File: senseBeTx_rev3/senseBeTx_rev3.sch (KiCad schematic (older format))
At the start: 44 parts, among them P1 CONN_02X05, Q1 SI2301, Q2 BC847, Q3 SI2302, Q4 SI2302, Q5 SI2302, Q6 SI2302, Q7 SI2302, SW1 SW_Push_Dual, U1 STM32L011F3Px, U2 AP3403, Y1 Crystal

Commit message: Done corrections in schematic.
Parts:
- removed D2: KPTBD-3216SURKCGKC, senseBeTx_rev1_fp:LED_KPTBD-3216SURKCGKC, symbol senseBeTx_rev3-rescue:LED_Dual_ACAC-senseBeRx_rev1
- removed Q2: BC847, Package_TO_SOT_SMD:SOT-23, symbol Device:Q_NPN_BEC
- removed Q3, Q4: SI2302, senseBeTx_rev1_fp:SOT-23, symbol Device:Q_NMOS_GSD
- removed R1: 10k, Resistor_SMD:R_0603_1608Metric_Pad1.05x0.95mm_HandSolder, symbol senseBeTx_rev3-rescue:R-senseBeRx_rev1
- removed R2, R5: 33E, Resistor_SMD:R_0603_1608Metric_Pad1.05x0.95mm_HandSolder, symbol senseBeTx_rev3-rescue:R-senseBeRx_rev1
- removed R6: 24E, Resistor_SMD:R_0603_1608Metric_Pad1.05x0.95mm_HandSolder, symbol senseBeTx_rev3-rescue:R-senseBeRx_rev1
- removed R7, R9: 100k, Resistor_SMD:R_0603_1608Metric_Pad1.05x0.95mm_HandSolder, symbol senseBeTx_rev3-rescue:R-senseBeRx_rev1
- added D2, D4, D5: LED, symbol Device:LED
- C6, C7, C8: symbol Ap3403_LED_test-rescue:C-AP3403_LED_test -> senseBeTx_rev3-rescue:C-AP3403_LED_test-Ap3403_LED_test-rescue
- D3: symbol Ap3403_LED_test-rescue:LED-AP3403_LED_test -> senseBeTx_rev3-rescue:LED-AP3403_LED_test-Ap3403_LED_test-rescue
- L1: symbol Ap3403_LED_test-rescue:L-AP3403_LED_test -> senseBeTx_rev3-rescue:L-AP3403_LED_test-Ap3403_LED_test-rescue
- Q5, Q6, Q7: symbol Ap3403_LED_test-rescue:Q_NMOS_GSD-AP3403_LED_test -> senseBeTx_rev3-rescue:Q_NMOS_GSD-AP3403_LED_test-Ap3403_LED_test-rescue
- R10: value 470k -> 510k; symbol Ap3403_LED_test-rescue:R-AP3403_LED_test -> senseBeTx_rev3-rescue:R-AP3403_LED_test-Ap3403_LED_test-rescue
- R11, R12, R13, R14, R15, R16, R8: symbol Ap3403_LED_test-rescue:R-AP3403_LED_test -> senseBeTx_rev3-rescue:R-AP3403_LED_test-Ap3403_LED_test-rescue
- SW1: symbol Switch:SW_SPST -> Switch:SW_DPST
- TP1: symbol Ap3403_LED_test-rescue:Test_Point-AP3403_LED_test -> senseBeTx_rev3-rescue:Test_Point-AP3403_LED_test-Ap3403_LED_test-rescue
- U2: symbol Ap3403_LED_test-rescue:AP3403-AP3403_LED_test -> senseBeTx_rev3-rescue:AP3403-AP3403_LED_test-Ap3403_LED_test-rescue
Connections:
- net labels added: IR_LED_EN, LED_RED_1, LED_RED_2, LED_RED_3, SENSE_CONTROL
- net labels removed: LED_EN, LED_GREEN, LED_RED, RXTX_UART_RX, RXTX_UART_TX, VIN
- wire segments 145 -> 127
- no-connect marks 0 -> 2
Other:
- note added: "3 Red LEDs\nfor Indication"
- note added: "Buck Regulator for IR LED\ninput Voltage/Current control."
- note removed: "Two color (Red/Green) LED"
- moved on the sheet: C2, C3, C4, C5, D1, MK1, MK2, P1, R3, R4, U1, Y1

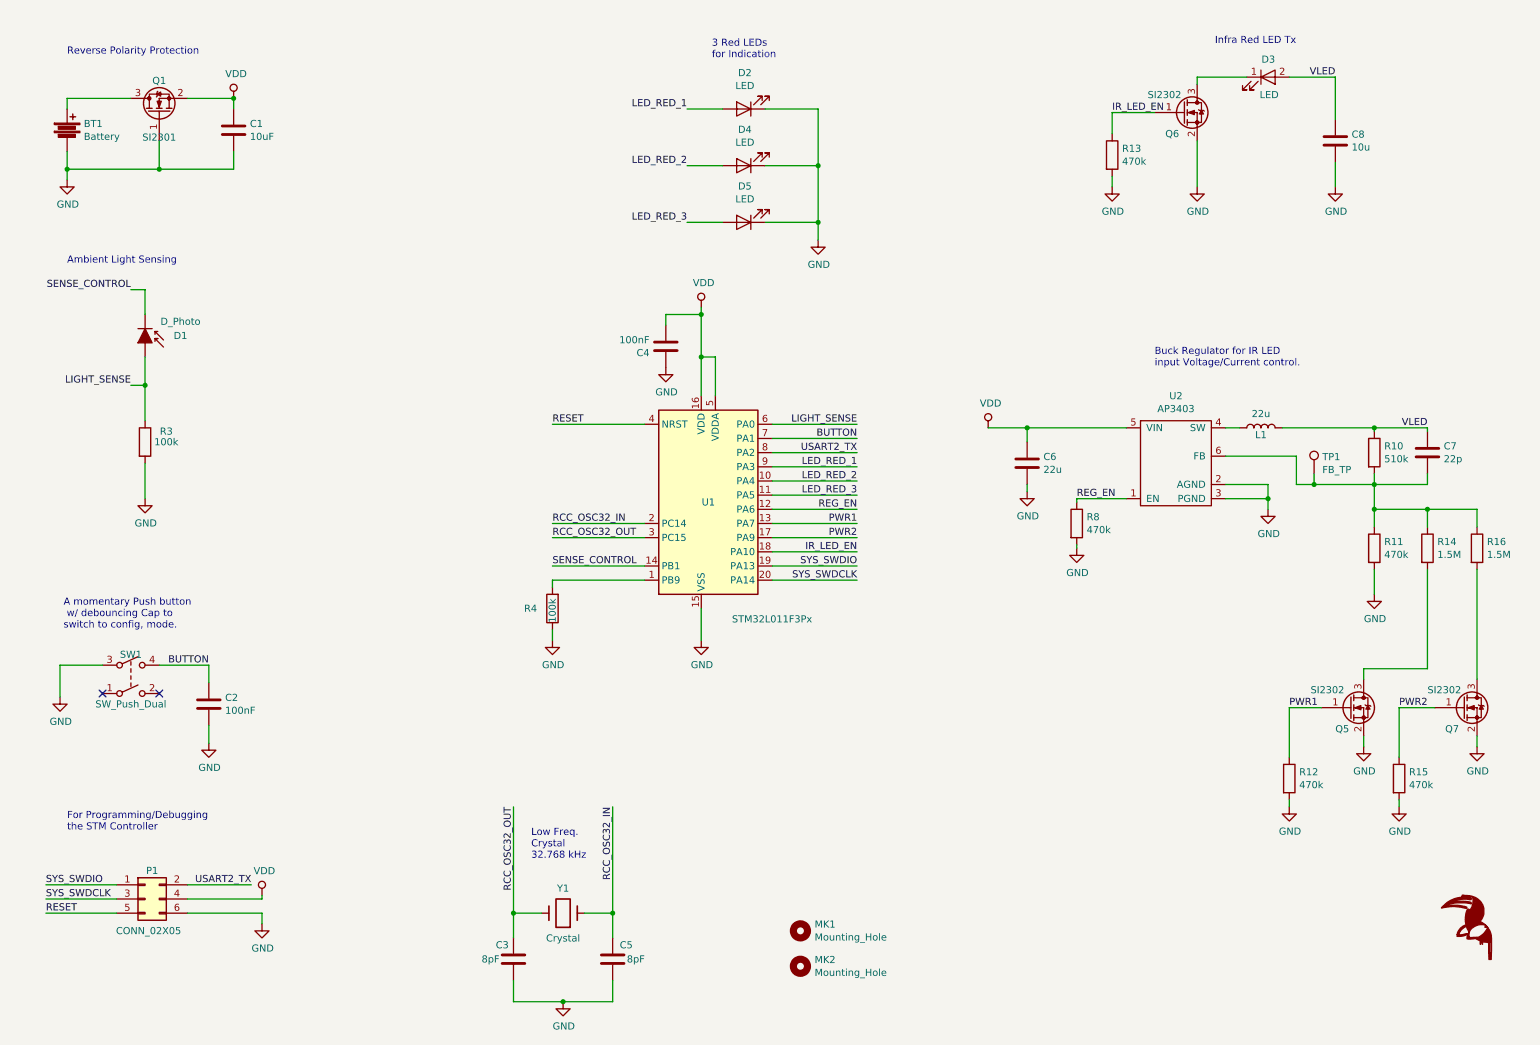
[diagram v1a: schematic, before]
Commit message: Updates PCB placement.
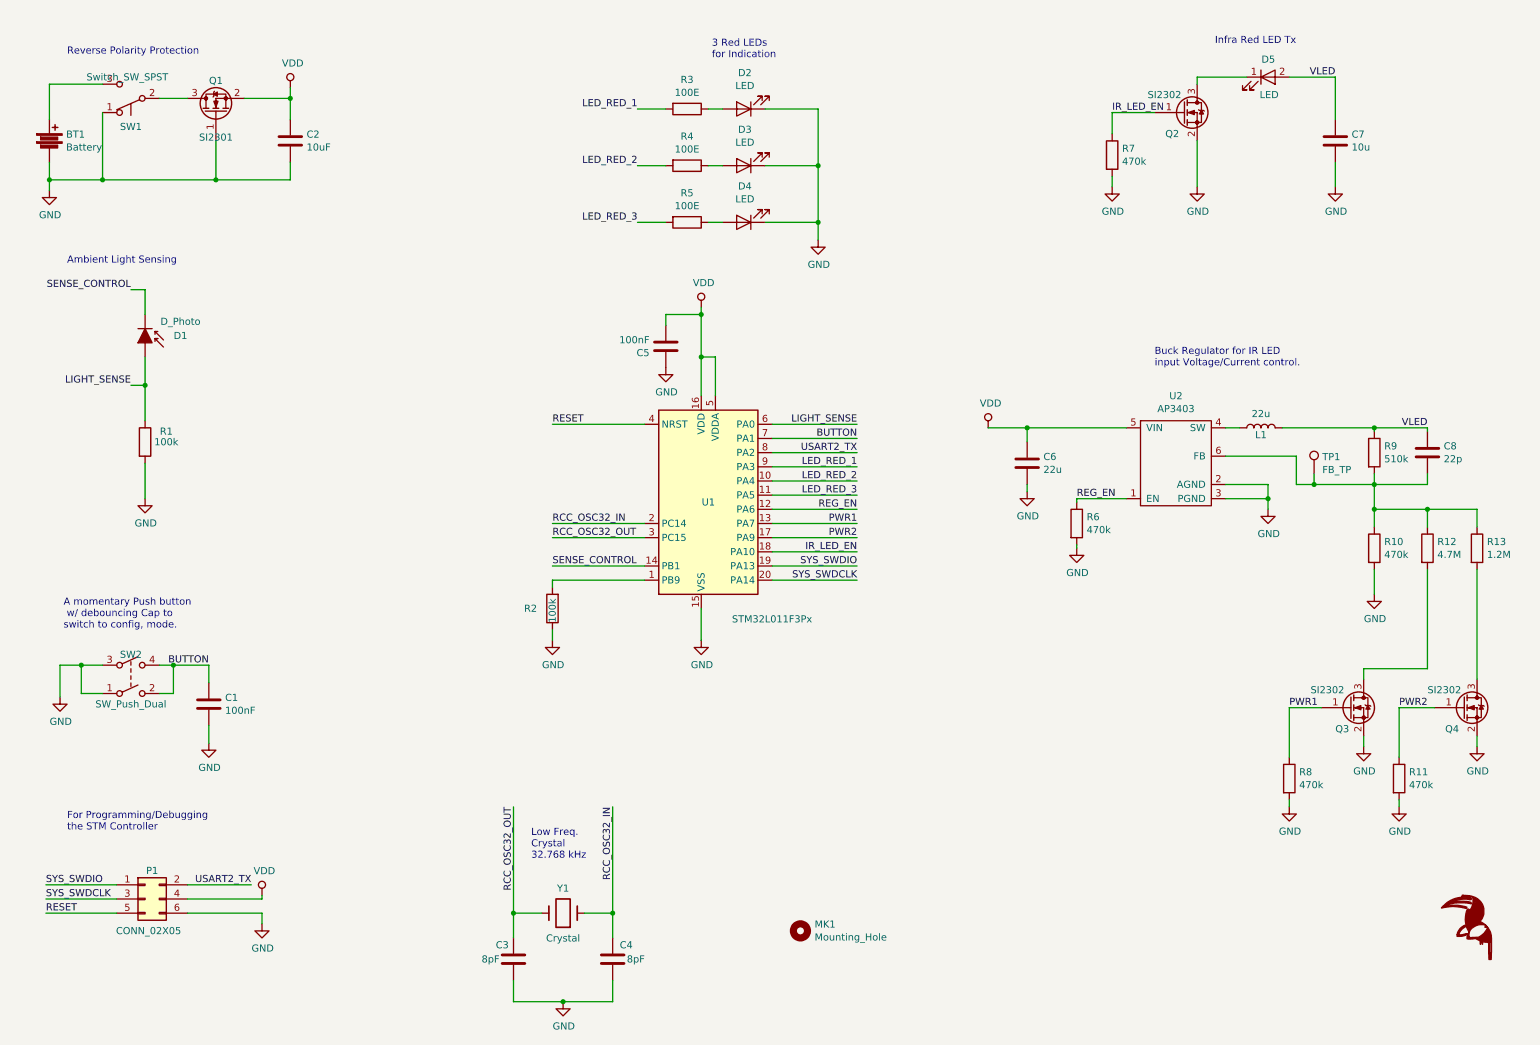
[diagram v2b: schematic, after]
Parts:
- removed MK2: Mounting_Hole, MountingHole:MountingHole_3.2mm_M3, symbol senseBeTx_rev3-rescue:Mounting_Hole-senseBeRx_rev1
- added R3, R4, R5: 100E, senseBeTx_rev3_fp:R_0603_HandSoldering, symbol Device:R
- added SW1: Switch_SW_SPST, senseBeTx_rev3_fp:SlideSwitch_1P2T_RightAngle, symbol Switch:SW_Push_SPDT
- BT1: footprint senseBeTx_rev2_fp:AA_BAT_Holder -> Connector_JST:JST_XH_S02B-XH-A_1x02_P2.50mm_Horizontal
- C2: renamed from C1; footprint senseBeTx_rev1_fp:C_0805 -> senseBeTx_rev3_fp:C_0805
- C6: footprint Ap3403_LED_test_fp:C_0805_HandSoldering -> senseBeTx_rev3_fp:C_0805_HandSoldering
- C7: renamed from C8; footprint Ap3403_LED_test_fp:C_0805_HandSoldering -> senseBeTx_rev3_fp:C_0805_HandSoldering
- C8: renamed from C7; footprint Ap3403_LED_test_fp:C_0603_HandSoldering -> senseBeTx_rev3_fp:C_0603_HandSoldering
- D2: footprint (none) -> LED_SMD:LED_0805_2012Metric
- D3: renamed from D4; footprint (none) -> LED_SMD:LED_0805_2012Metric
- D4: renamed from D5; footprint (none) -> LED_SMD:LED_0805_2012Metric
- P1: footprint senseBeTx_rev2_fp:prog_connect -> senseBeTx_rev3_fp:prog_connect_2x3
- Q1: footprint senseBeTx_rev1_fp:SOT-23 -> senseBeTx_rev3_fp:SOT-23_Handsoldering
- Q2: renamed from Q6; footprint Package_TO_SOT_SMD:SOT-23_Handsoldering -> senseBeTx_rev3_fp:SOT-23_Handsoldering
- Q3: renamed from Q5; footprint Package_TO_SOT_SMD:SOT-23_Handsoldering -> senseBeTx_rev3_fp:SOT-23_Handsoldering
- Q4: renamed from Q7; footprint Package_TO_SOT_SMD:SOT-23_Handsoldering -> senseBeTx_rev3_fp:SOT-23_Handsoldering
- R10: renamed from R11; footprint Ap3403_LED_test_fp:R_0603_HandSoldering -> senseBeTx_rev3_fp:R_0603_HandSoldering
- R11: renamed from R15; footprint Ap3403_LED_test_fp:R_0603_HandSoldering -> senseBeTx_rev3_fp:R_0603_HandSoldering
- R12: renamed from R14; value 1.5M -> 4.7M; footprint Ap3403_LED_test_fp:R_0603_HandSoldering -> senseBeTx_rev3_fp:R_0603_HandSoldering
- R13: renamed from R16; value 1.5M -> 1.2M; footprint Ap3403_LED_test_fp:R_0603_HandSoldering -> senseBeTx_rev3_fp:R_0603_HandSoldering
- R6: renamed from R8; footprint Ap3403_LED_test_fp:R_0603_HandSoldering -> senseBeTx_rev3_fp:R_0603_HandSoldering
- R7: renamed from R13; footprint Ap3403_LED_test_fp:R_0603_HandSoldering -> senseBeTx_rev3_fp:R_0603_HandSoldering
- R8: renamed from R12; footprint Ap3403_LED_test_fp:R_0603_HandSoldering -> senseBeTx_rev3_fp:R_0603_HandSoldering
- R9: renamed from R10; footprint Ap3403_LED_test_fp:R_0603_HandSoldering -> senseBeTx_rev3_fp:R_0603_HandSoldering
- TP1: footprint Ap3403_LED_test_fp:Measurement_Point_Round-SMD-Pad_Small -> senseBeTx_rev3_fp:Measurement_Point_Round-SMD-Pad_Small
- U2: footprint Ap3403_LED_test_fp:AP3403_U-DFN1616-6(Type G) -> senseBeTx_rev3_fp:AP3403_U-DFN1616-6(Type G)
- Y1: footprint senseBeTx_rev2_fp:Crystal_C38-LF_d3.0mm_l8.0mm_Vertical -> senseBeTx_rev3_fp:Crystal_C38-LF_d3.0mm_l8.0mm_Vertical
- renumbered C2 to C1, C5 to C4, C4 to C5, D3 to D5, R3 to R1, R4 to R2, SW1 to SW2
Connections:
- net BUTTON: now also SW2.2
- net GND: now also SW2.1, SW1.1 (A)
- net LED_RED_1: now also R3.2; no longer D2.2 (A)
- net LED_RED_2: now also R4.2; no longer D3.2 (A)
- net LED_RED_3: now also R5.2; no longer D4.2 (A)
- net at BT1.1: now also SW1.3 (C); no longer Q1.3 (D)
- new net: Q1.3 (D), SW1.2 (B)
- new net: D2.2 (A), R3.1
- new net: D3.2 (A), R4.1
- new net: D4.2 (A), R5.1
- no-connect marks 2 -> 0
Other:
- moved on the sheet: BT1, C2, Q1

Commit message: Updates the local libraries.
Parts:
- U1: symbol MCU_ST_STM32L0:STM32L011F3Px -> senseBeTx_rev3:MCU_ST_STM32L0_STM32L011F3Px
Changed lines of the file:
@@
 $EndComp
 $Comp
-L MCU_ST_STM32L0:STM32L011F3Px U1
+L senseBeTx_rev3:MCU_ST_STM32L0_STM32L011F3Px U1
 U 1 1 5BB21D50
 P 5525 3800
